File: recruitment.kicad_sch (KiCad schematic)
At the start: 4 parts, among them U1 ACS781LLRTR-050B-T

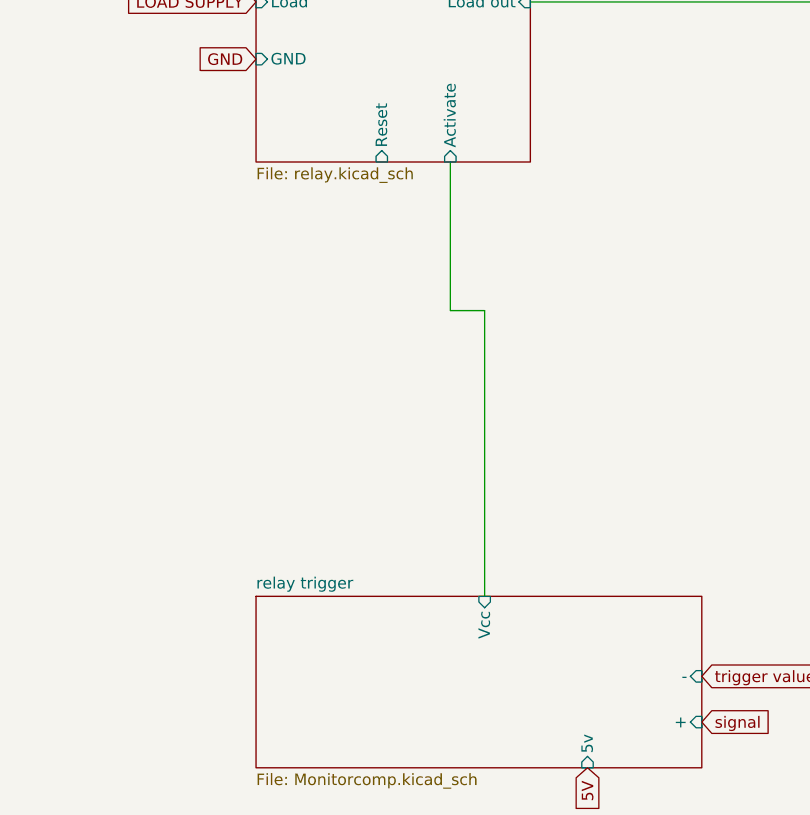
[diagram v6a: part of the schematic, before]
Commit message: POR implementation
added POR and fixed amplifier
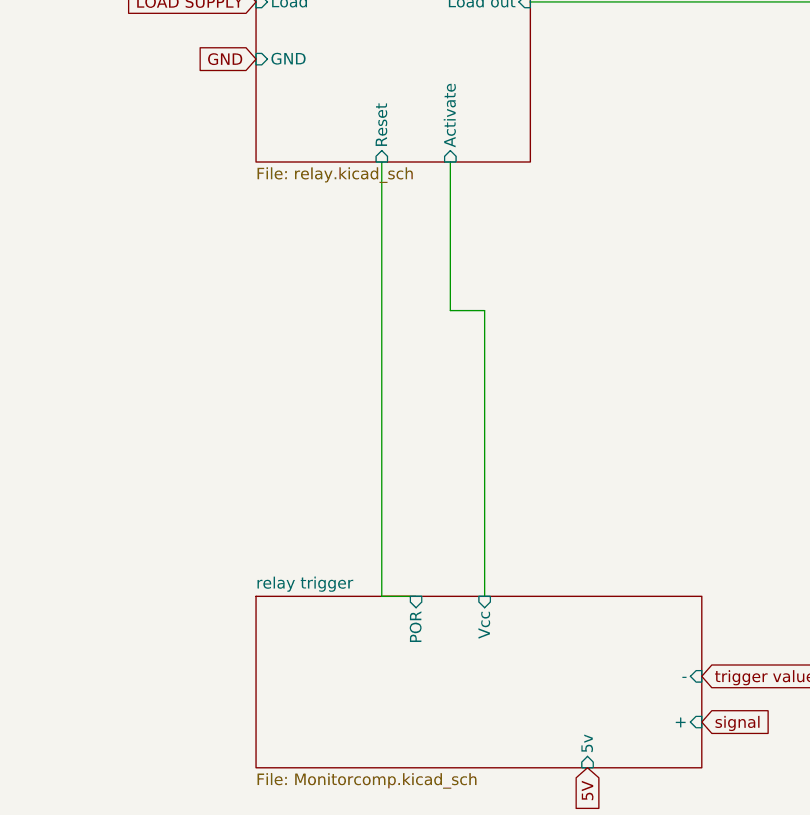
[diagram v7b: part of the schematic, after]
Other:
- sheet relay trigger ports: added POR; removed none
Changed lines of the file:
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@@
+	(wire
+		(pts
+			(xy 107.95 107.95) (xy 107.95 59.69)
+		)
+		(stroke
+			(width 0)
+			(type default)
+		)
+	)
 	(wire
 		(pts
@@
 		(pts
 			(xy 184.15 125.73) (xy 184.15 129.54)
+		)
+		(stroke
+			(width 0)
+			(type default)
+		)
+	)
+	(wire
+		(pts
+			(xy 111.76 107.95) (xy 107.95 107.95)
 		)
 		(stroke
@@
 			)
 		)
+		(pin "POR" input
+			(at 111.76 107.95 90)
+			(effects
+				(font
+					(size 1.27 1.27)
+				)
+				(justify right)
+			)
+		)
